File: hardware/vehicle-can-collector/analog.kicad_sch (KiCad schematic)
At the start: 9 parts, among them U601 AS2333Q

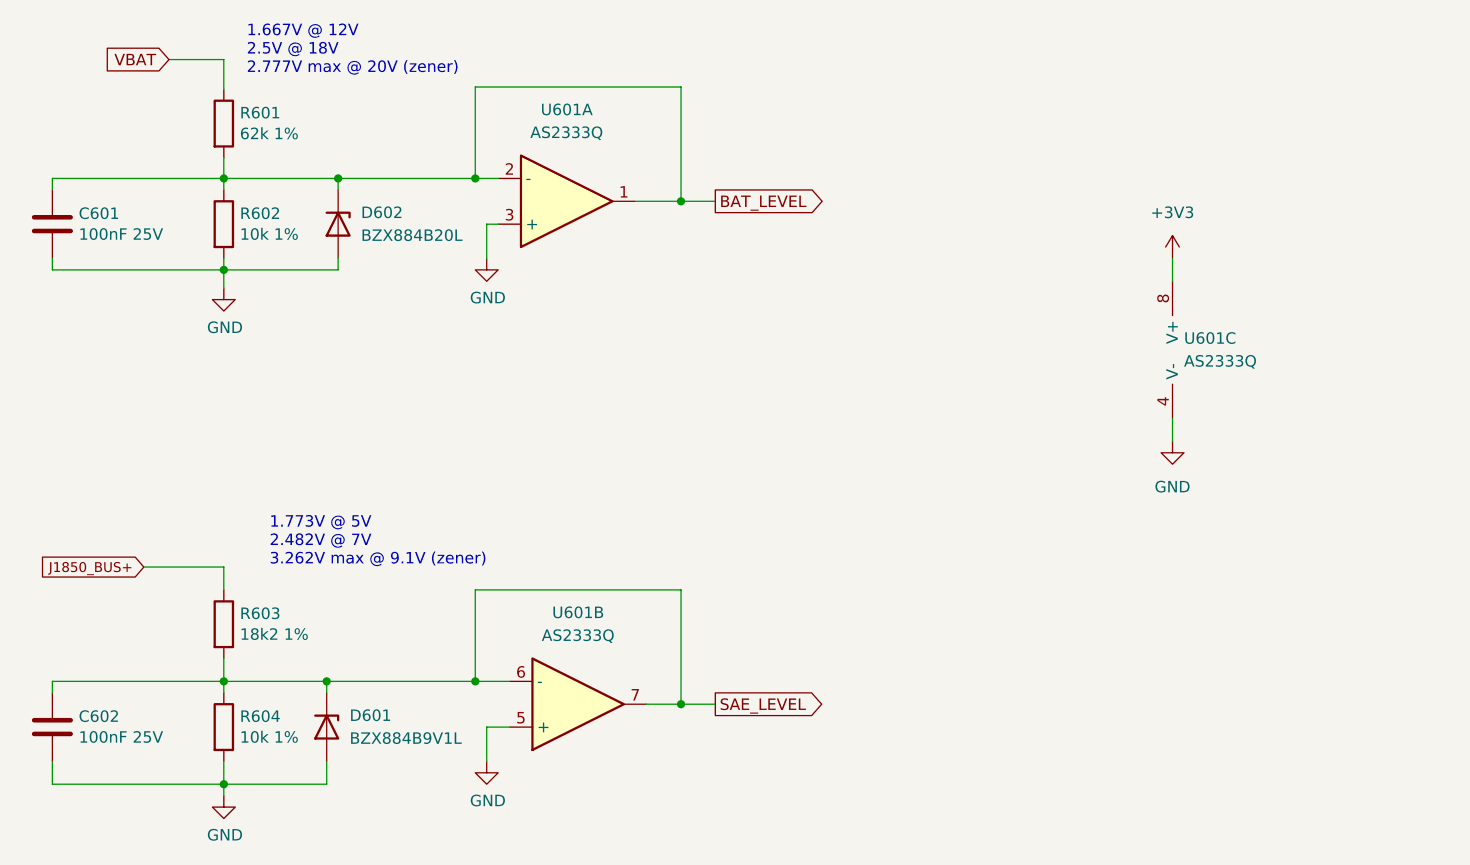
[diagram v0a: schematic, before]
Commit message: Added decoupling, more LEDs, update dts
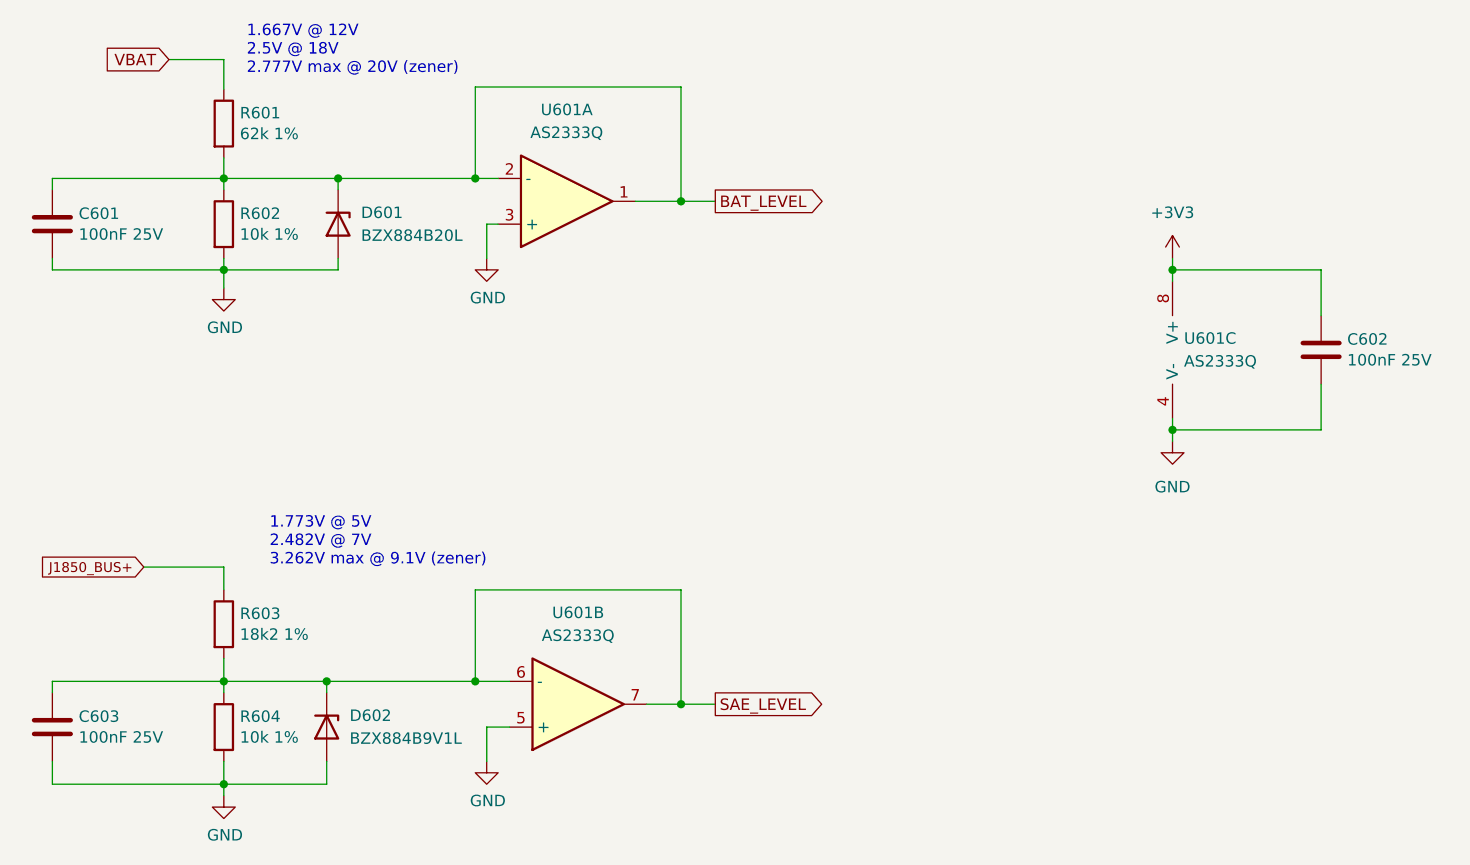
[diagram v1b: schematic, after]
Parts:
- added C602: 100nF 25V, symbol Device:C
- renumbered C602 to C603, D602 to D601, D601 to D602
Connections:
- net +3V3: now also C602.2
- net GND: now also C602.1
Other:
- company: (none) -> Gavin Hurlbut
- title: (none) -> Vehicle CAN Collector
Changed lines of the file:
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@@
 (kicad_sch (version 20211123) (generator eeschema)
   (paper "A4")
+  (title_block
+    (title "Vehicle CAN Collector")
+    (date "2022-12-29")
+    (rev "1")
+    (company "Gavin Hurlbut")
+  )
   (junction (at 116.84 130.81) (diameter 0) (color 0 0 0 0)
   )
   (junction (at 116.84 119.38) (diameter 0) (color 0 0 0 0)
   )
+  (junction (at 222.25 91.44) (diameter 0) (color 0 0 0 0)
+  )
   (junction (at 116.84 73.66) (diameter 0) (color 0 0 0 0)
   )
@@
   (junction (at 128.27 119.38) (diameter 0) (color 0 0 0 0)
   )
+  (junction (at 222.25 73.66) (diameter 0) (color 0 0 0 0)
+  )
   (junction (at 116.84 63.5) (diameter 0) (color 0 0 0 0)
   )
@@
     (stroke (width 0) (type default) (color 0 0 0 0))
   )
+  (wire (pts (xy 238.76 78.74) (xy 238.76 73.66))
+    (stroke (width 0) (type default) (color 0 0 0 0))
+  )
   (wire (pts (xy 116.84 130.81) (xy 128.27 130.81))
     (stroke (width 0) (type default) (color 0 0 0 0))
@@
     (stroke (width 0) (type default) (color 0 0 0 0))
   )
+  (wire (pts (xy 238.76 73.66) (xy 222.25 73.66))
+    (stroke (width 0) (type default) (color 0 0 0 0))
+  )
+  (wire (pts (xy 238.76 91.44) (xy 222.25 91.44))
+    (stroke (width 0) (type default) (color 0 0 0 0))
+  )
   (wire (pts (xy 116.84 50.292) (xy 116.84 53.594))
     (stroke (width 0) (type default) (color 0 0 0 0))
   )
+  (wire (pts (xy 222.25 91.44) (xy 222.25 92.71))
+    (stroke (width 0) (type default) (color 0 0 0 0))
+  )
   (wire (pts (xy 146.05 128.27) (xy 146.05 124.46))
     (stroke (width 0) (type default) (color 0 0 0 0))
@@
     (stroke (width 0) (type default) (color 0 0 0 0))
   )
+  (wire (pts (xy 238.76 86.36) (xy 238.76 91.44))
+    (stroke (width 0) (type default) (color 0 0 0 0))
+  )
   (wire (pts (xy 128.27 119.38) (xy 128.27 120.65))
     (stroke (width 0) (type default) (color 0 0 0 0))
@@
     (stroke (width 0) (type default) (color 0 0 0 0))
   )
-  (wire (pts (xy 222.25 72.39) (xy 222.25 74.93))
+  (wire (pts (xy 222.25 72.39) (xy 222.25 73.66))
     (stroke (width 0) (type default) (color 0 0 0 0))
   )
@@
     (stroke (width 0) (type default) (color 0 0 0 0))
   )
-  (wire (pts (xy 222.25 90.17) (xy 222.25 92.71))
+  (wire (pts (xy 222.25 90.17) (xy 222.25 91.44))
     (stroke (width 0) (type default) (color 0 0 0 0))
   )
@@
   )
   (wire (pts (xy 129.54 63.5) (xy 144.78 63.5))
+    (stroke (width 0) (type default) (color 0 0 0 0))
+  )
+  (wire (pts (xy 222.25 73.66) (xy 222.25 74.93))
     (stroke (width 0) (type default) (color 0 0 0 0))
   )
@@
   (symbol (lib_id "power:GND") (at 116.84 132.08 0) (unit 1)
     (in_bom yes) (on_board yes)
-    (property "Reference" "#PWR0602" (id 0) (at 116.84 138.43 0)
+    (property "Reference" "#PWR0606" (id 0) (at 116.84 138.43 0)
       (effects (font (size 1.27 1.27)) hide)
     )
@@
   (symbol (lib_id "power:GND") (at 116.84 75.692 0) (unit 1)
     (in_bom yes) (on_board yes)
-    (property "Reference" "#PWR0601" (id 0) (at 116.84 82.042 0)
+    (property "Reference" "#PWR0603" (id 0) (at 116.84 82.042 0)
       (effects (font (size 1.27 1.27)) hide)
     )
@@
   (symbol (lib_id "power:GND") (at 146.05 128.27 0) (unit 1)
     (in_bom yes) (on_board yes)
-    (property "Reference" "#PWR0604" (id 0) (at 146.05 134.62 0)
+    (property "Reference" "#PWR0605" (id 0) (at 146.05 134.62 0)
       (effects (font (size 1.27 1.27)) hide)
     )
@@
   (symbol (lib_id "power:GND") (at 146.05 72.39 0) (unit 1)
     (in_bom yes) (on_board yes)
-    (property "Reference" "#PWR0603" (id 0) (at 146.05 78.74 0)
+    (property "Reference" "#PWR0601" (id 0) (at 146.05 78.74 0)
       (effects (font (size 1.27 1.27)) hide)
     )
@@
   (symbol (lib_id "Device:D_Zener") (at 128.27 124.46 270) (unit 1)
     (in_bom yes) (on_board yes) (fields_autoplaced)
-    (property "Reference" "D601" (id 0) (at 130.81 123.1899 90)
+    (property "Reference" "D602" (id 0) (at 130.81 123.1899 90)
       (effects (font (size 1.27 1.27)) (justify left))
     )
@@
   (symbol (lib_id "Device:C") (at 97.79 124.46 0) (unit 1)
     (in_bom yes) (on_board yes)
-    (property "Reference" "C602" (id 0) (at 100.711 123.2916 0)
+    (property "Reference" "C603" (id 0) (at 100.711 123.2916 0)
       (effects (font (size 1.27 1.27)) (justify left))
     )
@@
     (pin "7")
   )
+  (symbol (lib_id "Device:C") (at 238.76 82.55 180) (unit 1)
+    (in_bom yes) (on_board yes)
+    (property "Reference" "C602" (id 0) (at 241.6556 81.3816 0)
+      (effects (font (size 1.27 1.27)) (justify right))
+    )
+    (property "Value" "100nF 25V" (id 1) (at 241.6556 83.693 0)
+      (effects (font (size 1.27 1.27)) (justify right))
+    )
+    (property "Footprint" "" (id 2) (at 237.7948 78.74 0)
+      (effects (font (size 1.27 1.27)) hide)
+    )
+    (property "Datasheet" "~" (id 3) (at 238.76 82.55 0)
+      (effects (font (size 1.27 1.27)) hide)
+    )
+    (pin "1")
+    (pin "2")
+  )
   (symbol (lib_id "Device:D_Zener") (at 129.54 68.58 270) (unit 1)
     (in_bom yes) (on_board yes) (fields_autoplaced)
-    (property "Reference" "D602" (id 0) (at 132.08 67.3099 90)
+    (property "Reference" "D601" (id 0) (at 132.08 67.3099 90)
       (effects (font (size 1.27 1.27)) (justify left))
     )
@@
   (symbol (lib_id "power:+3V3") (at 222.25 72.39 0) (unit 1)
     (in_bom yes) (on_board yes) (fields_autoplaced)
-    (property "Reference" "#PWR0605" (id 0) (at 222.25 76.2 0)
+    (property "Reference" "#PWR0602" (id 0) (at 222.25 76.2 0)
       (effects (font (size 1.27 1.27)) hide)
     )
@@
   (symbol (lib_id "power:GND") (at 222.25 92.71 0) (unit 1)
     (in_bom yes) (on_board yes) (fields_autoplaced)
-    (property "Reference" "#PWR0606" (id 0) (at 222.25 99.06 0)
-      (effects (font (size 1.27 1.27)) hide)
-    )
+    (property "Reference" "#PWR0604" (id 0) (at 222.25 99.06 0)
+      (effects (font (size 1.27 1.27)) hide)
+    )

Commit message: Added footprints, tossed all footprints onto PCB
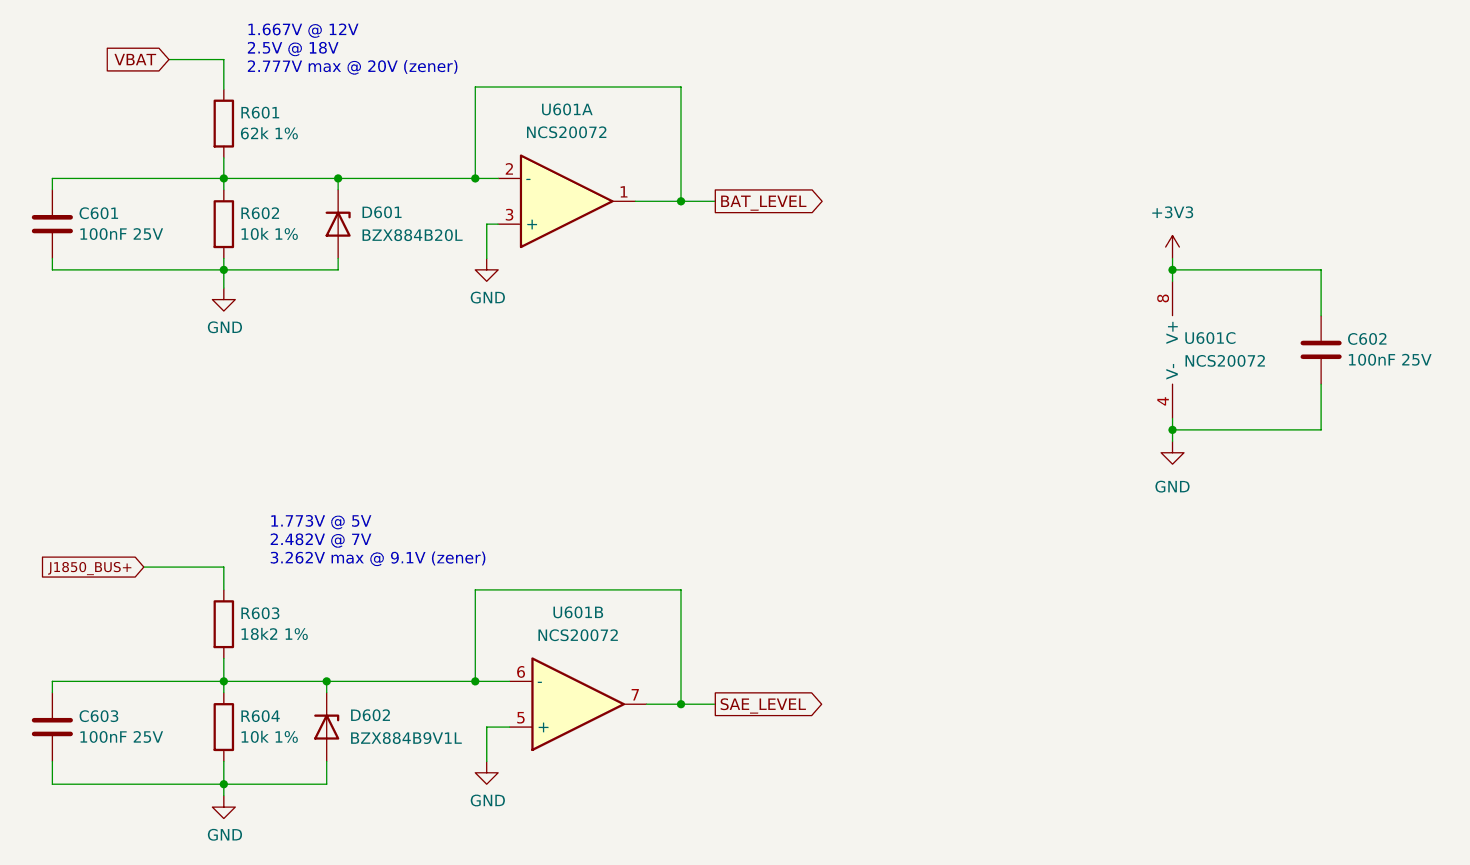
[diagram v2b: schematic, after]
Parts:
- C601, C602, C603: footprint (none) -> Capacitor_SMD:C_0805_2012Metric_Pad1.18x1.45mm_HandSolder
- R601, R602, R603, R604: footprint (none) -> Resistor_SMD:R_0805_2012Metric_Pad1.20x1.40mm_HandSolder
- U601: value AS2333Q -> NCS20072; footprint Package_SO:SOIC-8_3.9x4.9mm_P1.27mm -> Package_SO:TSSOP-8_4.4x3mm_P0.65mm
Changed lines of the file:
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@@
       (effects (font (size 1.27 1.27)) (justify left))
     )
-    (property "Footprint" "" (id 2) (at 115.062 124.46 90)
+    (property "Footprint" "Resistor_SMD:R_0805_2012Metric_Pad1.20x1.40mm_HandSolder" (id 2) (at 115.062 124.46 90)
       (effects (font (size 1.27 1.27)) hide)
     )
@@
       (effects (font (size 1.27 1.27)) (justify left))
     )
-    (property "Footprint" "" (id 2) (at 115.062 68.58 90)
+    (property "Footprint" "Resistor_SMD:R_0805_2012Metric_Pad1.20x1.40mm_HandSolder" (id 2) (at 115.062 68.58 90)
       (effects (font (size 1.27 1.27)) hide)
     )
@@
       (effects (font (size 1.27 1.27)) (justify left))
     )
-    (property "Footprint" "" (id 2) (at 115.062 57.404 90)
+    (property "Footprint" "Resistor_SMD:R_0805_2012Metric_Pad1.20x1.40mm_HandSolder" (id 2) (at 115.062 57.404 90)
       (effects (font (size 1.27 1.27)) hide)
     )
@@
       (effects (font (size 1.27 1.27)) (justify left))
     )
-    (property "Footprint" "" (id 2) (at 98.7552 72.39 0)
+    (property "Footprint" "Capacitor_SMD:C_0805_2012Metric_Pad1.18x1.45mm_HandSolder" (id 2) (at 98.7552 72.39 0)
       (effects (font (size 1.27 1.27)) hide)
     )
@@
       (effects (font (size 1.27 1.27)) (justify left))
     )
-    (property "Footprint" "" (id 2) (at 115.062 113.03 90)
+    (property "Footprint" "Resistor_SMD:R_0805_2012Metric_Pad1.20x1.40mm_HandSolder" (id 2) (at 115.062 113.03 90)
       (effects (font (size 1.27 1.27)) hide)
     )
@@
       (effects (font (size 1.27 1.27)) (justify left))
     )
-    (property "Value" "AS2333Q" (id 1) (at 223.52 83.8199 0)
-      (effects (font (size 1.27 1.27)) (justify left))
-    )
-    (property "Footprint" "Package_SO:SOIC-8_3.9x4.9mm_P1.27mm" (id 2) (at 224.79 82.55 0)
+    (property "Value" "NCS20072" (id 1) (at 223.52 83.8199 0)
+      (effects (font (size 1.27 1.27)) (justify left))
+    )
+    (property "Footprint" "Package_SO:TSSOP-8_4.4x3mm_P0.65mm" (id 2) (at 224.79 82.55 0)
       (effects (font (size 1.27 1.27)) hide)
     )
@@
       (effects (font (size 1.27 1.27)) (justify left))
     )
-    (property "Footprint" "" (id 2) (at 98.7552 128.27 0)
+    (property "Footprint" "Capacitor_SMD:C_0805_2012Metric_Pad1.18x1.45mm_HandSolder" (id 2) (at 98.7552 128.27 0)
       (effects (font (size 1.27 1.27)) hide)
     )
@@
     (in_bom yes) (on_board yes) (fields_autoplaced)
     (property "Reference" "U601" (id 0) (at 154.94 55.88 0))
-    (property "Value" "AS2333Q" (id 1) (at 154.94 58.42 0))
-    (property "Footprint" "Package_SO:SOIC-8_3.9x4.9mm_P1.27mm" (id 2) (at 154.94 66.04 0)
+    (property "Value" "NCS20072" (id 1) (at 154.94 58.42 0))
+    (property "Footprint" "Package_SO:TSSOP-8_4.4x3mm_P0.65mm" (id 2) (at 154.94 66.04 0)
       (effects (font (size 1.27 1.27)) hide)
     )
@@
     (in_bom yes) (on_board yes) (fields_autoplaced)
     (property "Reference" "U601" (id 0) (at 156.21 111.76 0))
-    (property "Value" "AS2333Q" (id 1) (at 156.21 114.3 0))
-    (property "Footprint" "Package_SO:SOIC-8_3.9x4.9mm_P1.27mm" (id 2) (at 156.21 121.92 0)
+    (property "Value" "NCS20072" (id 1) (at 156.21 114.3 0))
+    (property "Footprint" "Package_SO:TSSOP-8_4.4x3mm_P0.65mm" (id 2) (at 156.21 121.92 0)
       (effects (font (size 1.27 1.27)) hide)
     )
@@
       (effects (font (size 1.27 1.27)) (justify right))
     )
-    (property "Footprint" "" (id 2) (at 237.7948 78.74 0)
-      (effects (font (size 1.27 1.27)) hide)
-    )
+    (property "Footprint" "Capacitor_SMD:C_0805_2012Metric_Pad1.18x1.45mm_HandSolder" (id 2) (at 237.7948 78.74 0)
+      (effects (font (size 1.27 1.27)) hide)
+    )
